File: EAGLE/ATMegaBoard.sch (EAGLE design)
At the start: 28 parts, among them IC1 L298, IC2 ATMEGA168-20P, IC3 REG1117, J1 1X2-3.5MM, J2 1X2-3.5MM, J3 1X2-3.5MM, J4 1X2-3.5MM, X1 49S/18PF

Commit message: added standalone board
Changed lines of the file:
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@@
 <wire x1="127" y1="-12.7" x2="127" y2="2.54" width="0.1524" layer="91"/>
 <wire x1="127" y1="-12.7" x2="114.3" y2="-12.7" width="0.1524" layer="91"/>
-<wire x1="114.3" y1="-12.7" x2="114.3" y2="-30.48" width="0.1524" layer="91"/>
-<wire x1="114.3" y1="-30.48" x2="254" y2="-30.48" width="0.1524" layer="91"/>
-<wire x1="254" y1="-30.48" x2="254" y2="73.66" width="0.1524" layer="91"/>
+<wire x1="114.3" y1="-12.7" x2="114.3" y2="-27.94" width="0.1524" layer="91"/>
+<wire x1="114.3" y1="-27.94" x2="243.84" y2="-27.94" width="0.1524" layer="91"/>
+<wire x1="243.84" y1="-27.94" x2="243.84" y2="73.66" width="0.1524" layer="91"/>
 <pinref part="D1" gate="1" pin="C"/>
 <wire x1="177.8" y1="63.5" x2="177.8" y2="73.66" width="0.1524" layer="91"/>
@@
 <wire x1="210.82" y1="73.66" x2="200.66" y2="73.66" width="0.1524" layer="91"/>
 <junction x="200.66" y="73.66"/>
-<wire x1="254" y1="73.66" x2="210.82" y2="73.66" width="0.1524" layer="91"/>
+<wire x1="243.84" y1="73.66" x2="210.82" y2="73.66" width="0.1524" layer="91"/>
 <junction x="210.82" y="73.66"/>
 <wire x1="170.18" y1="60.96" x2="170.18" y2="73.66" width="0.1524" layer="91"/>

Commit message: updated ATMegaBoard, added CAM files
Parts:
- renumbered J1 to OUT1, J2 to OUT2, J3 to OUT3, J4 to OUT4
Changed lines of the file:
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@@
 <part name="LED1" library="led" library_urn="urn:adsk.eagle:library:259" deviceset="LED" device="5MM" package3d_urn="urn:adsk.eagle:package:15799/2"/>
 <part name="VIN" library="con-jack" library_urn="urn:adsk.eagle:library:154" deviceset="JACK-PLUG" device="1" package3d_urn="urn:adsk.eagle:package:7494/1"/>
-<part name="J1" library="adafruit" deviceset="1X2" device="-3.5MM"/>
-<part name="J2" library="adafruit" deviceset="1X2" device="-3.5MM"/>
-<part name="J3" library="adafruit" deviceset="1X2" device="-3.5MM"/>
-<part name="J4" library="adafruit" deviceset="1X2" device="-3.5MM"/>
+<part name="OUT1" library="adafruit" deviceset="1X2" device="-3.5MM"/>
+<part name="OUT2" library="adafruit" deviceset="1X2" device="-3.5MM"/>
+<part name="OUT3" library="adafruit" deviceset="1X2" device="-3.5MM"/>
+<part name="OUT4" library="adafruit" deviceset="1X2" device="-3.5MM"/>
 <part name="D1" library="adafruit" deviceset="1N4004" device=""/>
 <part name="D2" library="adafruit" deviceset="1N4004" device=""/>
@@
 <attribute name="VALUE" x="134.62" y="-25.4" size="1.778" layer="96" rot="R90"/>
 </instance>
-<instance part="J1" gate="G$1" x="236.22" y="48.26" smashed="yes"/>
-<instance part="J2" gate="G$1" x="236.22" y="38.1" smashed="yes"/>
-<instance part="J3" gate="G$1" x="236.22" y="27.94" smashed="yes"/>
-<instance part="J4" gate="G$1" x="236.22" y="17.78" smashed="yes"/>
+<instance part="OUT1" gate="G$1" x="236.22" y="48.26" smashed="yes"/>
+<instance part="OUT2" gate="G$1" x="236.22" y="38.1" smashed="yes"/>
+<instance part="OUT3" gate="G$1" x="236.22" y="27.94" smashed="yes"/>
+<instance part="OUT4" gate="G$1" x="236.22" y="17.78" smashed="yes"/>
 <instance part="D1" gate="1" x="177.8" y="60.96" smashed="yes" rot="R90">
 <attribute name="NAME" x="177.3174" y="63.5" size="1.778" layer="95" rot="R90"/>
@@
 </segment>
 <segment>
-<pinref part="J1" gate="G$1" pin="2"/>
+<pinref part="OUT1" gate="G$1" pin="2"/>
 <wire x1="231.14" y1="48.26" x2="228.6" y2="48.26" width="0.1524" layer="91"/>
 <label x="228.6" y="48.26" size="1.778" layer="95"/>
 </segment>
 <segment>
-<pinref part="J2" gate="G$1" pin="2"/>
+<pinref part="OUT2" gate="G$1" pin="2"/>
 <wire x1="231.14" y1="38.1" x2="228.6" y2="38.1" width="0.1524" layer="91"/>
 <label x="228.6" y="38.1" size="1.778" layer="95"/>
 </segment>
 <segment>
-<pinref part="J3" gate="G$1" pin="2"/>
+<pinref part="OUT3" gate="G$1" pin="2"/>
 <wire x1="231.14" y1="27.94" x2="228.6" y2="27.94" width="0.1524" layer="91"/>
 <label x="228.6" y="27.94" size="1.778" layer="95"/>
 </segment>
 <segment>
-<pinref part="J4" gate="G$1" pin="2"/>
+<pinref part="OUT4" gate="G$1" pin="2"/>
 <wire x1="231.14" y1="17.78" x2="228.6" y2="17.78" width="0.1524" layer="91"/>
 <label x="228.6" y="17.78" size="1.778" layer="95"/>
@@
 <label x="226.06" y="50.8" size="1.778" layer="95"/>
 <wire x1="167.64" y1="48.26" x2="167.64" y2="50.8" width="0.1524" layer="91"/>
-<pinref part="J1" gate="G$1" pin="1"/>
+<pinref part="OUT1" gate="G$1" pin="1"/>
 <wire x1="167.64" y1="50.8" x2="177.8" y2="50.8" width="0.1524" layer="91"/>
 <pinref part="D1" gate="1" pin="A"/>
@@
 <segment>
 <pinref part="IC1" gate="L298" pin="OUT2"/>
-<pinref part="J2" gate="G$1" pin="1"/>
+<pinref part="OUT2" gate="G$1" pin="1"/>
 <wire x1="162.56" y1="45.72" x2="185.42" y2="45.72" width="0.1524" layer="91"/>
 <wire x1="185.42" y1="45.72" x2="231.14" y2="45.72" width="0.1524" layer="91"/>
@@
 <wire x1="193.04" y1="43.18" x2="226.06" y2="43.18" width="0.1524" layer="91"/>
 <wire x1="226.06" y1="43.18" x2="226.06" y2="30.48" width="0.1524" layer="91"/>
-<pinref part="J3" gate="G$1" pin="1"/>
+<pinref part="OUT3" gate="G$1" pin="1"/>
 <wire x1="226.06" y1="30.48" x2="231.14" y2="30.48" width="0.1524" layer="91"/>
 <label x="162.56" y="43.18" size="1.778" layer="95"/>
@@
 <wire x1="200.66" y1="40.64" x2="223.52" y2="40.64" width="0.1524" layer="91"/>
 <wire x1="223.52" y1="40.64" x2="223.52" y2="20.32" width="0.1524" layer="91"/>
-<pinref part="J4" gate="G$1" pin="1"/>
+<pinref part="OUT4" gate="G$1" pin="1"/>
 <wire x1="223.52" y1="20.32" x2="231.14" y2="20.32" width="0.1524" layer="91"/>
 <label x="162.56" y="40.64" size="1.778" layer="95"/>

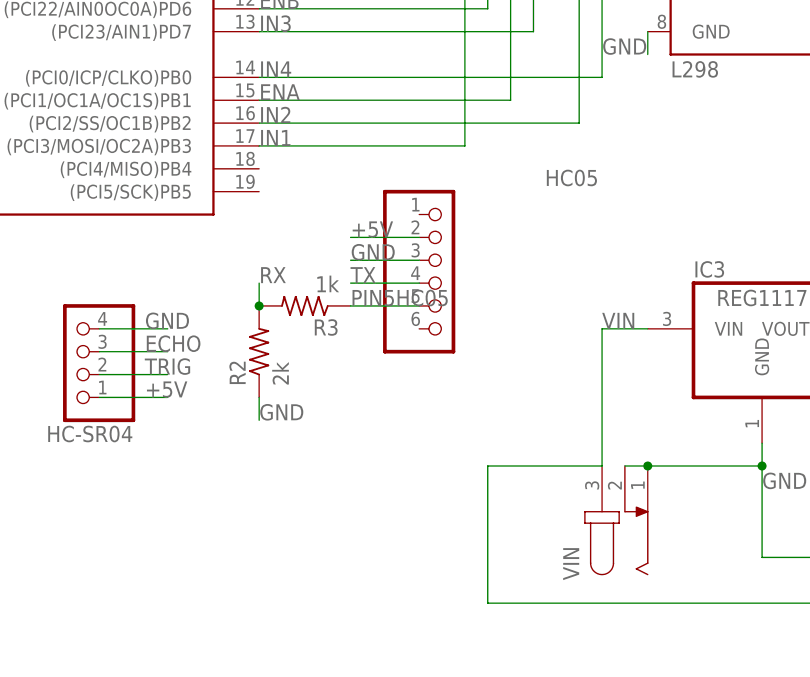
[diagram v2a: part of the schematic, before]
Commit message: Switched to female header for HC05
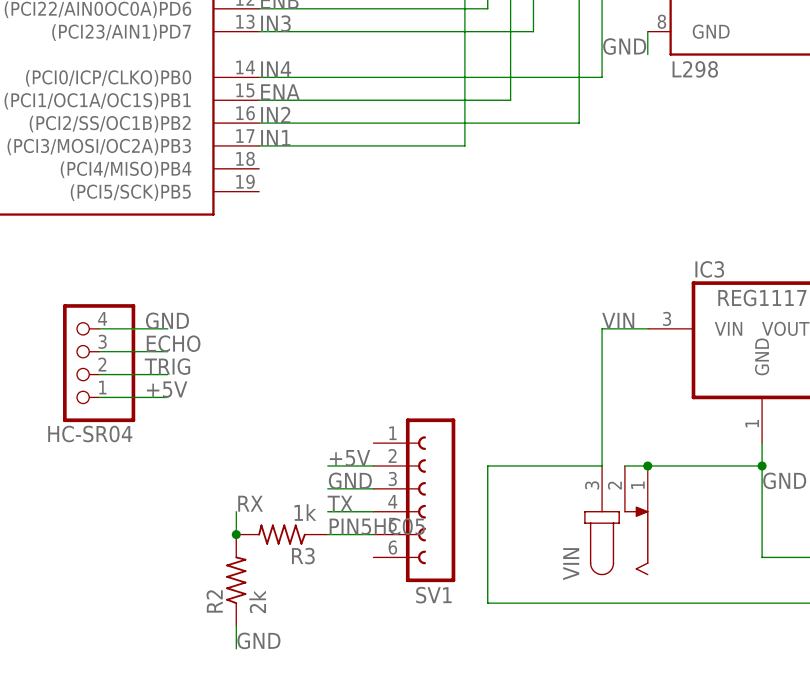
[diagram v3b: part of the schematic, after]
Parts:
- removed HC05: (no value), pinhead:PINHD-1X6/90
- added SV1: (no value), con-lsta:FE06W
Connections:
- net +5V: now also SV1.2; no longer HC05.2
- net GND: now also SV1.3; no longer HC05.3
- net PIN5HC05: now also SV1.5; no longer HC05.5
- net TX: now also SV1.4; no longer HC05.4
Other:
- moved on the sheet: R2, R3
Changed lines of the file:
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@@
 <part name="X_3" library="ngspice-simulation" library_urn="urn:adsk.eagle:library:527439" deviceset="GND" device=""/>
 <part name="IC1" library="st-microelectronics" library_urn="urn:adsk.eagle:library:368" deviceset="L298" device="" package3d_urn="urn:adsk.eagle:package:26823/1"/>
-<part name="HC05" library="pinhead" library_urn="urn:adsk.eagle:library:325" deviceset="PINHD-1X6" device="/90" package3d_urn="urn:adsk.eagle:package:22475/2"/>
 <part name="HC-SR04" library="pinhead" library_urn="urn:adsk.eagle:library:325" deviceset="PINHD-1X4" device="" package3d_urn="urn:adsk.eagle:package:22407/2"/>
 <part name="SG90" library="pinhead" library_urn="urn:adsk.eagle:library:325" deviceset="PINHD-1X3" device="" package3d_urn="urn:adsk.eagle:package:22458/2"/>
@@
 <part name="R2" library="rcl" library_urn="urn:adsk.eagle:library:334" deviceset="R-US_" device="0207/10" package3d_urn="urn:adsk.eagle:package:23491/2" value="2k"/>
 <part name="R3" library="rcl" library_urn="urn:adsk.eagle:library:334" deviceset="R-US_" device="0207/10" package3d_urn="urn:adsk.eagle:package:23491/2" value="1k"/>
+<part name="SV1" library="con-lsta" library_urn="urn:adsk.eagle:library:161" deviceset="FE06W" device="" package3d_urn="urn:adsk.eagle:package:8198/1"/>
 </parts>
 <sheets>
@@
 <attribute name="VALUE" x="134.62" y="30.48" size="1.778" layer="96"/>
 </instance>
-<instance part="HC05" gate="A" x="109.22" y="7.62" smashed="yes">
-<attribute name="NAME" x="120.65" y="18.415" size="1.778" layer="95"/>
-<attribute name="VALUE" x="102.87" y="-2.54" size="1.778" layer="96"/>
-</instance>
 <instance part="HC-SR04" gate="A" x="68.58" y="0" smashed="yes" rot="R180">
 <attribute name="NAME" x="74.93" y="-8.255" size="1.778" layer="95" rot="R180"/>
@@
 <attribute name="VALUE" x="211.836" y="56.769" size="1.778" layer="96"/>
 </instance>
-<instance part="R2" gate="G$1" x="88.9" y="0" smashed="yes" rot="R90">
-<attribute name="NAME" x="87.4014" y="-3.81" size="1.778" layer="95" rot="R90"/>
-<attribute name="VALUE" x="92.202" y="-3.81" size="1.778" layer="96" rot="R90"/>
-</instance>
-<instance part="R3" gate="G$1" x="93.98" y="5.08" smashed="yes" rot="R180">
-<attribute name="NAME" x="97.79" y="3.5814" size="1.778" layer="95" rot="R180"/>
-<attribute name="VALUE" x="97.79" y="8.382" size="1.778" layer="96" rot="R180"/>
+<instance part="R2" gate="G$1" x="86.36" y="-25.4" smashed="yes" rot="R90">
+<attribute name="NAME" x="84.8614" y="-29.21" size="1.778" layer="95" rot="R90"/>
+<attribute name="VALUE" x="89.662" y="-29.21" size="1.778" layer="96" rot="R90"/>
+</instance>
+<instance part="R3" gate="G$1" x="91.44" y="-20.32" smashed="yes" rot="R180">
+<attribute name="NAME" x="95.25" y="-21.8186" size="1.778" layer="95" rot="R180"/>
+<attribute name="VALUE" x="95.25" y="-17.018" size="1.778" layer="96" rot="R180"/>
+</instance>
+<instance part="SV1" gate="G$1" x="109.22" y="-15.24" smashed="yes" rot="R180">
+<attribute name="VALUE" x="110.49" y="-5.08" size="1.778" layer="96" rot="R180"/>
+<attribute name="NAME" x="110.49" y="-26.162" size="1.778" layer="95" rot="R180"/>
 </instance>
 </instances>
@@
 <pinref part="R3" gate="G$1" pin="2"/>
 <pinref part="R2" gate="G$1" pin="2"/>
-<wire x1="88.9" y1="5.08" x2="88.9" y2="7.62" width="0.1524" layer="91"/>
-<junction x="88.9" y="5.08"/>
-<label x="88.9" y="7.62" size="1.778" layer="95"/>
+<wire x1="86.36" y1="-20.32" x2="86.36" y2="-17.78" width="0.1524" layer="91"/>
+<junction x="86.36" y="-20.32"/>
+<label x="86.36" y="-17.78" size="1.778" layer="95"/>
 </segment>
 </net>
 <net name="TX" class="0">
-<segment>
-<pinref part="HC05" gate="A" pin="4"/>
-<wire x1="106.68" y1="7.62" x2="99.06" y2="7.62" width="0.1524" layer="91"/>
-<label x="99.06" y="7.62" size="1.778" layer="95"/>
-</segment>
 <segment>
 <pinref part="IC2" gate="G$1" pin="(PCI16/RXD)PD0"/>
@@
 <label x="88.9" y="53.34" size="1.778" layer="95"/>
 </segment>
+<segment>
+<pinref part="SV1" gate="G$1" pin="4"/>
+<wire x1="101.6" y1="-17.78" x2="96.52" y2="-17.78" width="0.1524" layer="91"/>
+<label x="96.52" y="-17.78" size="1.778" layer="95"/>
+</segment>
 </net>
 <net name="+5V" class="2">
-<segment>
-<pinref part="HC05" gate="A" pin="2"/>
-<wire x1="106.68" y1="12.7" x2="99.06" y2="12.7" width="0.1524" layer="91"/>
-<label x="99.06" y="12.7" size="1.778" layer="95"/>
-</segment>
 <segment>
 <pinref part="IC2" gate="G$1" pin="VCC"/>
@@
 <junction x="162.56" y="2.54"/>
 </segment>
+<segment>
+<pinref part="SV1" gate="G$1" pin="2"/>
+<wire x1="101.6" y1="-12.7" x2="96.52" y2="-12.7" width="0.1524" layer="91"/>
+<label x="96.52" y="-12.7" size="1.778" layer="95"/>
+</segment>
 </net>
 <net name="GND" class="1">
-<segment>
-<pinref part="HC05" gate="A" pin="3"/>
-<wire x1="106.68" y1="10.16" x2="99.06" y2="10.16" width="0.1524" layer="91"/>
-<label x="99.06" y="10.16" size="1.778" layer="95"/>
-</segment>
 <segment>
 <label x="27.94" y="48.26" size="1.778" layer="95"/>
@@
 <segment>
 <pinref part="R2" gate="G$1" pin="1"/>
-<wire x1="88.9" y1="-5.08" x2="88.9" y2="-7.62" width="0.1524" layer="91"/>
-<label x="88.9" y="-7.62" size="1.778" layer="95"/>
+<wire x1="86.36" y1="-30.48" x2="86.36" y2="-33.02" width="0.1524" layer="91"/>
+<label x="86.36" y="-33.02" size="1.778" layer="95"/>
+</segment>
+<segment>
+<pinref part="SV1" gate="G$1" pin="3"/>
+<wire x1="101.6" y1="-15.24" x2="96.52" y2="-15.24" width="0.1524" layer="91"/>
+<label x="96.52" y="-15.24" size="1.778" layer="95"/>
 </segment>
 </net>
@@
 <net name="PIN5HC05" class="0">
 <segment>
-<pinref part="HC05" gate="A" pin="5"/>
-<wire x1="106.68" y1="5.08" x2="99.06" y2="5.08" width="0.1524" layer="91"/>
-<label x="99.06" y="5.08" size="1.778" layer="95"/>
+<pinref part="SV1" gate="G$1" pin="5"/>
+<wire x1="101.6" y1="-20.32" x2="96.52" y2="-20.32" width="0.1524" layer="91"/>
+<label x="96.52" y="-20.32" size="1.778" layer="95"/>
 <pinref part="R3" gate="G$1" pin="1"/>
 </segment>

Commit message: compressed board
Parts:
- renumbered SV1 to HC05
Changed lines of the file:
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@@
 <part name="R2" library="rcl" library_urn="urn:adsk.eagle:library:334" deviceset="R-US_" device="0207/10" package3d_urn="urn:adsk.eagle:package:23491/2" value="2k"/>
 <part name="R3" library="rcl" library_urn="urn:adsk.eagle:library:334" deviceset="R-US_" device="0207/10" package3d_urn="urn:adsk.eagle:package:23491/2" value="1k"/>
-<part name="SV1" library="con-lsta" library_urn="urn:adsk.eagle:library:161" deviceset="FE06W" device="" package3d_urn="urn:adsk.eagle:package:8198/1"/>
+<part name="HC05" library="con-lsta" library_urn="urn:adsk.eagle:library:161" deviceset="FE06W" device="" package3d_urn="urn:adsk.eagle:package:8198/1"/>
 </parts>
 <sheets>
@@
 <attribute name="VALUE" x="95.25" y="-17.018" size="1.778" layer="96" rot="R180"/>
 </instance>
-<instance part="SV1" gate="G$1" x="109.22" y="-15.24" smashed="yes" rot="R180">
+<instance part="HC05" gate="G$1" x="109.22" y="-15.24" smashed="yes" rot="R180">
 <attribute name="VALUE" x="110.49" y="-5.08" size="1.778" layer="96" rot="R180"/>
 <attribute name="NAME" x="110.49" y="-26.162" size="1.778" layer="95" rot="R180"/>
@@
 </segment>
 <segment>
-<pinref part="SV1" gate="G$1" pin="4"/>
+<pinref part="HC05" gate="G$1" pin="4"/>
 <wire x1="101.6" y1="-17.78" x2="96.52" y2="-17.78" width="0.1524" layer="91"/>
 <label x="96.52" y="-17.78" size="1.778" layer="95"/>
@@
 </segment>
 <segment>
-<pinref part="SV1" gate="G$1" pin="2"/>
+<pinref part="HC05" gate="G$1" pin="2"/>
 <wire x1="101.6" y1="-12.7" x2="96.52" y2="-12.7" width="0.1524" layer="91"/>
 <label x="96.52" y="-12.7" size="1.778" layer="95"/>
@@
 </segment>
 <segment>
-<pinref part="SV1" gate="G$1" pin="3"/>
+<pinref part="HC05" gate="G$1" pin="3"/>
 <wire x1="101.6" y1="-15.24" x2="96.52" y2="-15.24" width="0.1524" layer="91"/>
 <label x="96.52" y="-15.24" size="1.778" layer="95"/>
@@
 <net name="PIN5HC05" class="0">
 <segment>
-<pinref part="SV1" gate="G$1" pin="5"/>
+<pinref part="HC05" gate="G$1" pin="5"/>
 <wire x1="101.6" y1="-20.32" x2="96.52" y2="-20.32" width="0.1524" layer="91"/>
 <label x="96.52" y="-20.32" size="1.778" layer="95"/>

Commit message: minor board updates
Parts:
- added LIGHTS: (no value), con-lstb:MA05-2
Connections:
- new net N$1: IC2.(PCI8/ADC0)PC0, LIGHTS.3, LIGHTS.4
- new net N$2: IC2.(PCI9/ADC1)PC1, LIGHTS.5, LIGHTS.6
- new net N$4: IC2.(PCI10/ADC2)PC2, LIGHTS.7, LIGHTS.8
- new net N$5: IC2.(PCI11/ADC3)PC3, LIGHTS.10, LIGHTS.9
- net +5V: now also IC2.PC6(/RESET/PCI14)
- net GND: now also LIGHTS.1, LIGHTS.2
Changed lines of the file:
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@@
 <part name="R3" library="rcl" library_urn="urn:adsk.eagle:library:334" deviceset="R-US_" device="0207/10" package3d_urn="urn:adsk.eagle:package:23491/2" value="1k"/>
 <part name="HC05" library="con-lsta" library_urn="urn:adsk.eagle:library:161" deviceset="FE06W" device="" package3d_urn="urn:adsk.eagle:package:8198/1"/>
+<part name="LIGHTS" library="con-lstb" library_urn="urn:adsk.eagle:library:162" deviceset="MA05-2" device="" package3d_urn="urn:adsk.eagle:package:8329/1"/>
 </parts>
 <sheets>
@@
 <attribute name="NAME" x="110.49" y="-26.162" size="1.778" layer="95" rot="R180"/>
 </instance>
+<instance part="LIGHTS" gate="G$1" x="114.3" y="76.2" smashed="yes" rot="R180">
+<attribute name="VALUE" x="118.11" y="86.36" size="1.778" layer="96" rot="R180"/>
+<attribute name="NAME" x="118.11" y="67.818" size="1.778" layer="95" rot="R180"/>
+</instance>
 </instances>
 <busses>
@@
 <wire x1="101.6" y1="-12.7" x2="96.52" y2="-12.7" width="0.1524" layer="91"/>
 <label x="96.52" y="-12.7" size="1.778" layer="95"/>
+</segment>
+<segment>
+<pinref part="IC2" gate="G$1" pin="PC6(/RESET/PCI14)"/>
+<wire x1="33.02" y1="78.74" x2="25.4" y2="78.74" width="0.1524" layer="91"/>
+<wire x1="25.4" y1="78.74" x2="25.4" y2="81.28" width="0.1524" layer="91"/>
+<label x="25.4" y="81.28" size="1.778" layer="95"/>
 </segment>
 </net>
@@
 <wire x1="101.6" y1="-15.24" x2="96.52" y2="-15.24" width="0.1524" layer="91"/>
 <label x="96.52" y="-15.24" size="1.778" layer="95"/>
+</segment>
+<segment>
+<pinref part="LIGHTS" gate="G$1" pin="1"/>
+<wire x1="106.68" y1="81.28" x2="106.68" y2="86.36" width="0.1524" layer="91"/>
+<wire x1="106.68" y1="86.36" x2="114.3" y2="86.36" width="0.1524" layer="91"/>
+<pinref part="LIGHTS" gate="G$1" pin="2"/>
+<wire x1="114.3" y1="86.36" x2="121.92" y2="86.36" width="0.1524" layer="91"/>
+<wire x1="121.92" y1="86.36" x2="121.92" y2="81.28" width="0.1524" layer="91"/>
+<wire x1="114.3" y1="86.36" x2="114.3" y2="88.9" width="0.1524" layer="91"/>
+<junction x="114.3" y="86.36"/>
+<label x="114.3" y="88.9" size="1.778" layer="95"/>
 </segment>
 </net>
@@
 </segment>
 </net>
+<net name="N$1" class="0">
+<segment>
+<pinref part="IC2" gate="G$1" pin="(PCI8/ADC0)PC0"/>
+<pinref part="LIGHTS" gate="G$1" pin="3"/>
+<wire x1="88.9" y1="78.74" x2="106.68" y2="78.74" width="0.1524" layer="91"/>
+<pinref part="LIGHTS" gate="G$1" pin="4"/>
+<wire x1="106.68" y1="78.74" x2="121.92" y2="78.74" width="0.1524" layer="91"/>
+<junction x="106.68" y="78.74"/>
+</segment>
+</net>
+<net name="N$2" class="0">
+<segment>
+<pinref part="IC2" gate="G$1" pin="(PCI9/ADC1)PC1"/>
+<pinref part="LIGHTS" gate="G$1" pin="5"/>
+<wire x1="88.9" y1="76.2" x2="106.68" y2="76.2" width="0.1524" layer="91"/>
+<pinref part="LIGHTS" gate="G$1" pin="6"/>
+<wire x1="106.68" y1="76.2" x2="121.92" y2="76.2" width="0.1524" layer="91"/>
+<junction x="106.68" y="76.2"/>
+</segment>
+</net>
+<net name="N$4" class="0">
+<segment>
+<pinref part="IC2" gate="G$1" pin="(PCI10/ADC2)PC2"/>
+<pinref part="LIGHTS" gate="G$1" pin="7"/>
+<wire x1="88.9" y1="73.66" x2="106.68" y2="73.66" width="0.1524" layer="91"/>
+<pinref part="LIGHTS" gate="G$1" pin="8"/>
+<wire x1="106.68" y1="73.66" x2="121.92" y2="73.66" width="0.1524" layer="91"/>
+<junction x="106.68" y="73.66"/>
+</segment>
+</net>
+<net name="N$5" class="0">
+<segment>
+<pinref part="IC2" gate="G$1" pin="(PCI11/ADC3)PC3"/>
+<pinref part="LIGHTS" gate="G$1" pin="9"/>
+<wire x1="88.9" y1="71.12" x2="106.68" y2="71.12" width="0.1524" layer="91"/>
+<pinref part="LIGHTS" gate="G$1" pin="10"/>
+<wire x1="106.68" y1="71.12" x2="121.92" y2="71.12" width="0.1524" layer="91"/>
+<junction x="106.68" y="71.12"/>
+</segment>
+</net>
